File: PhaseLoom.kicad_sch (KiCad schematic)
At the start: 77 parts, among them J1 NC, J1 RF_IN, J2 LO_CLK, J2 NC, J3 CLK2, J3 I_OUT, J4 Q_OUT, J5 LO_CLK+90, Q1 AO3400A, Q2 AO3400A, SW1 USR1, SW2 USR2, SW3 USR3, SW4 USR4, SW5 USR5, T1 50:200, U1 74CBTLV3253PW, U2 ADA4891-2, U3 Si5351A-B-GTR, U5 MIC5504-3.3YM5, Y1 25Mhz

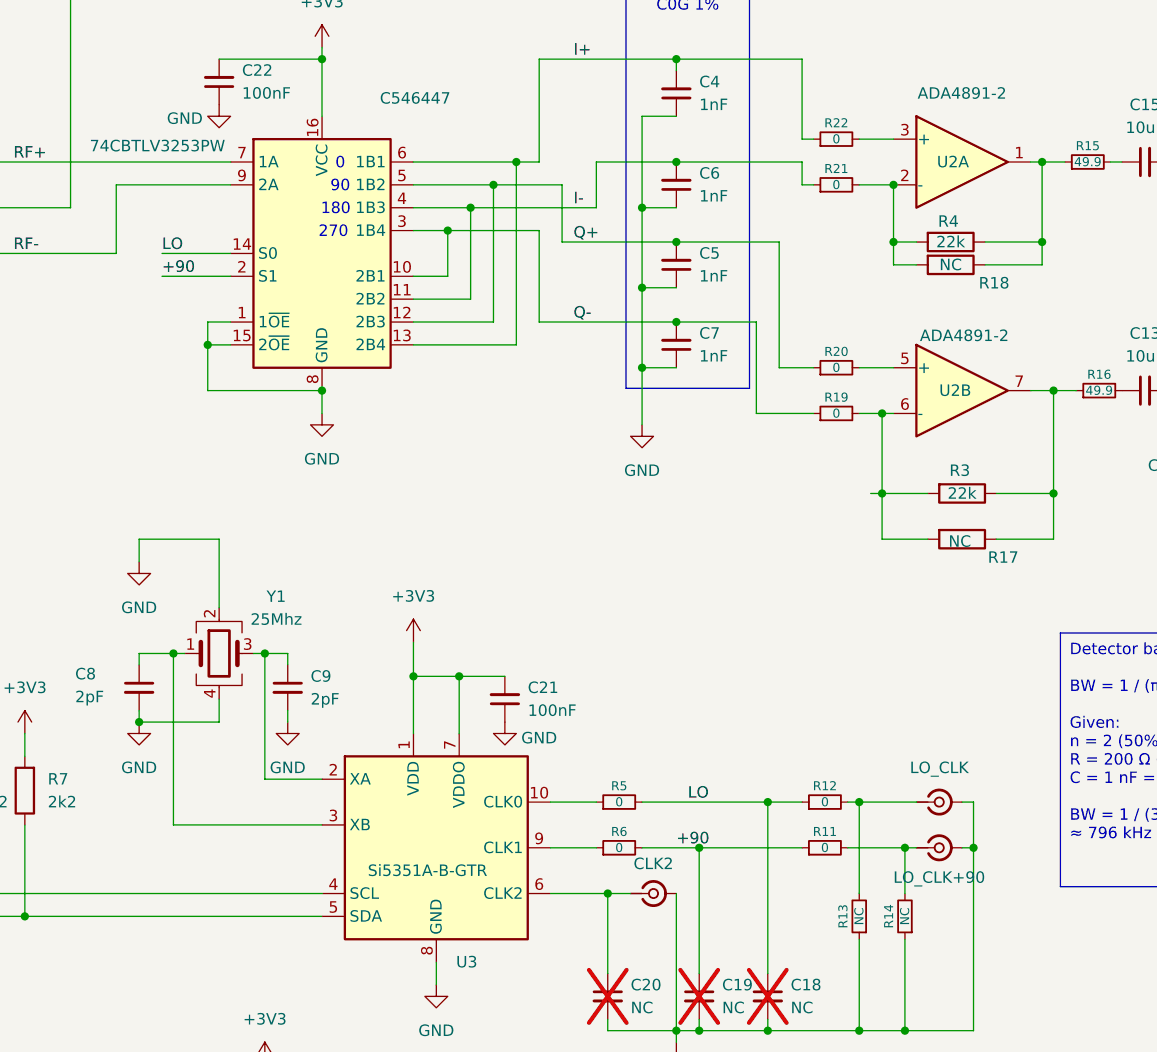
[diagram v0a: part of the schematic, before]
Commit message: v1.1 Fix: Swap I- and Q-, improve stitching
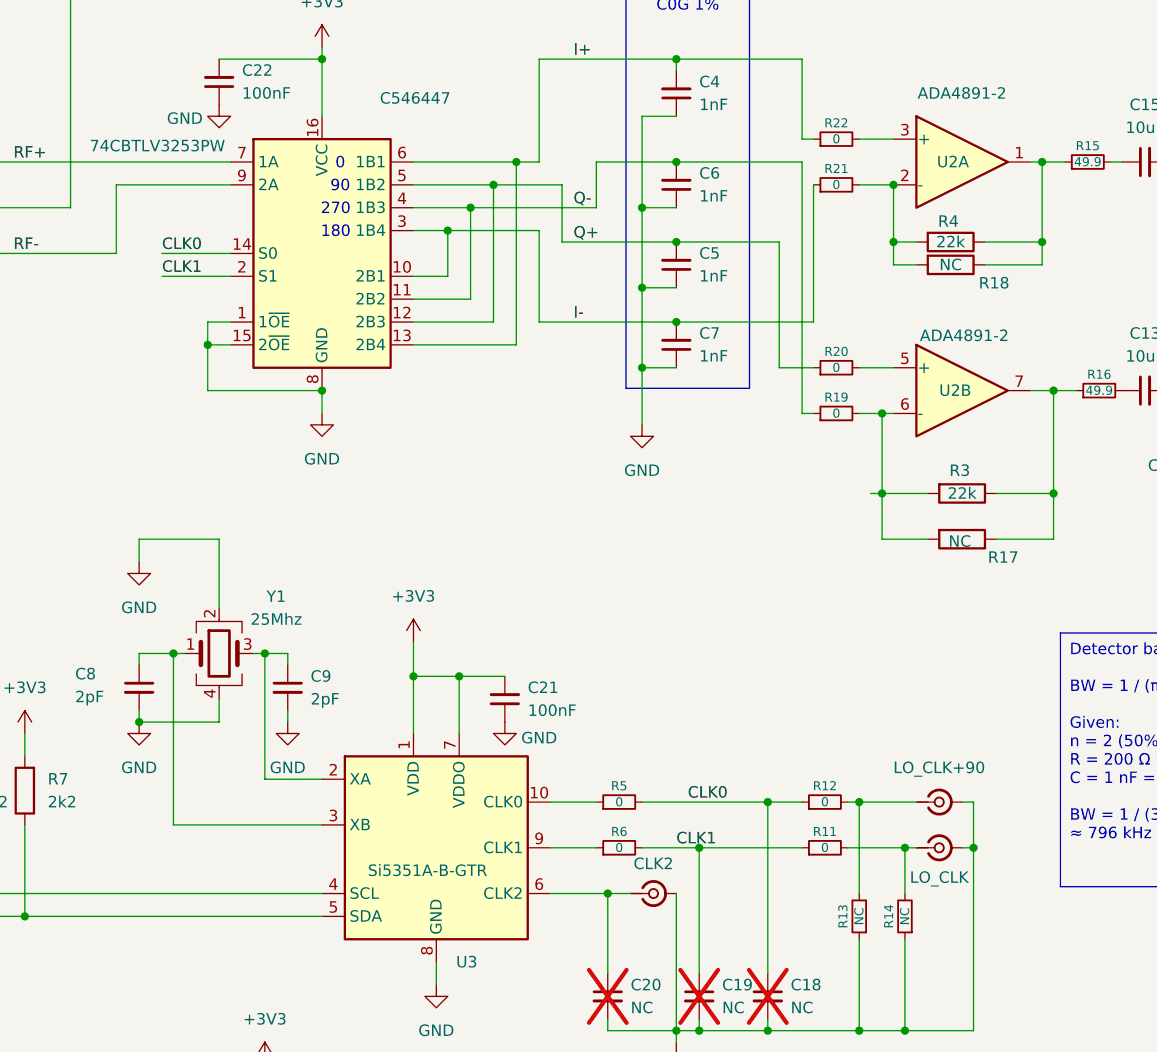
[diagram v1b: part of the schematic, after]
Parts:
- J2: value LO_CLK -> LO_CLK+90
- J5: value LO_CLK+90 -> LO_CLK
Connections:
- net I-: now also C7.2, U1.10 (2B1), U1.3 (1B4); no longer C6.2, U1.11 (2B2), U1.4 (1B3)
- net Q-: now also C6.2, U1.11 (2B2), U1.4 (1B3); no longer C7.2, U1.10 (2B1), U1.3 (1B4)
- net +90 renamed CLK1
- net LO renamed CLK0
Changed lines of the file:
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@@
 		(title "PhaseLoom")
 		(date "2025-06-05")
-		(rev "A")
+		(rev "v1.1")
 		(company "iMania.dk")
 		(comment 1 "Quadrature Sampling Detector  Phase Locked Loop LO Synthesizer SDR Frontend")
@@
 	(wire
 		(pts
+			(xy 160.02 62.23) (xy 160.02 90.17)
+		)
+		(stroke
+			(width 0)
+			(type default)
+		)
+	)
+	(wire
+		(pts
 			(xy 228.6 63.5) (xy 231.14 63.5)
 		)
@@
 	(wire
 		(pts
-			(xy 160.02 62.23) (xy 160.02 64.77)
-		)
-		(stroke
-			(width 0)
-			(type default)
-		)
-	)
-	(wire
-		(pts
 			(xy 96.52 184.15) (xy 82.55 184.15)
 		)
@@
 	(wire
 		(pts
-			(xy 154.94 80.01) (xy 154.94 90.17)
+			(xy 161.29 80.01) (xy 161.29 64.77)
 		)
 		(stroke
@@
 	(wire
 		(pts
-			(xy 154.94 90.17) (xy 161.29 90.17)
+			(xy 160.02 90.17) (xy 161.29 90.17)
 		)
 		(stroke
@@
 	(wire
 		(pts
-			(xy 161.29 64.77) (xy 160.02 64.77)
-		)
-		(stroke
-			(width 0)
-			(type default)
-		)
-	)
-	(wire
-		(pts
 			(xy 168.91 104.14) (xy 168.91 99.06)
 		)
@@
 	(wire
 		(pts
-			(xy 146.05 80.01) (xy 154.94 80.01)
+			(xy 146.05 80.01) (xy 161.29 80.01)
 		)
 		(stroke
@@
 	(text "270"
 		(exclude_from_sim no)
-		(at 107.95 70.104 0)
+		(at 108.204 67.564 0)
 		(effects
 			(font
@@
 	(text "180"
 		(exclude_from_sim no)
-		(at 108.204 67.564 0)
+		(at 108.204 70.104 0)
 		(effects
 			(font
@@
 	)
 	(label "Q-"
-		(at 134.62 80.01 0)
+		(at 134.62 67.31 0)
 		(fields_autoplaced yes)
 		(effects
@@
 	)
 	(label "I-"
-		(at 134.62 67.31 0)
+		(at 134.62 80.01 0)
 		(fields_autoplaced yes)
 		(effects
@@
 		)
 	)
-	(label "LO"
+	(label "CLK0"
 		(at 88.9 72.39 0)
 		(fields_autoplaced yes)
@@
 		)
 	)
-	(label "LO"
+	(label "CLK0"
 		(at 147.32 133.35 0)
 		(fields_autoplaced yes)
@@
 		)
 	)
-	(label "+90"
+	(label "CLK1"
 		(at 146.05 138.43 0)
 		(fields_autoplaced yes)
@@
 		)
 	)
-	(label "+90"
+	(label "CLK1"
 		(at 88.9 74.93 0)
 		(fields_autoplaced yes)
@@
 			)
 		)
-		(property "Value" "LO_CLK"
+		(property "Value" "LO_CLK+90"
 			(at 175.26 129.54 0)
 			(effects
@@
 			)
 		)
-		(property "Value" "LO_CLK+90"
+		(property "Value" "LO_CLK"
 			(at 175.26 141.732 0)
 			(effects

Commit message: Documentation and images
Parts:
- A1: value Arduino_UNO_R3 -> 65uino
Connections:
- net GND: no longer C18.2, C19.2, C20.2, J2.2 (Ext), J3.2 (Ext), J5.2 (Ext), R13.1, R14.1
- new net: C18.2, C19.2, C20.2, J2.2 (Ext), J3.2 (Ext), J5.2 (Ext), R13.1, R14.1
- no-connect marks 10 -> 9
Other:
- moved on the sheet: C1, C10, C11, C12, C13, C14, C15, C16, C17, C18, C19, C2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
